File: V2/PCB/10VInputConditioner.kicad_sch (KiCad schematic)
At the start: 3 parts

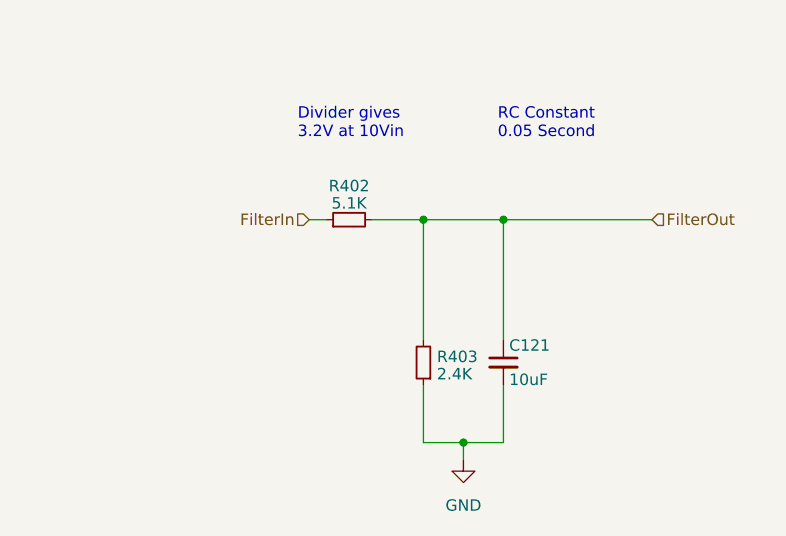
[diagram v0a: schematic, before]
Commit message: Changed ADC divider
Changed ADC divider to give 1.9v for 10V in this matches up with the 2.048v input range on the ADC
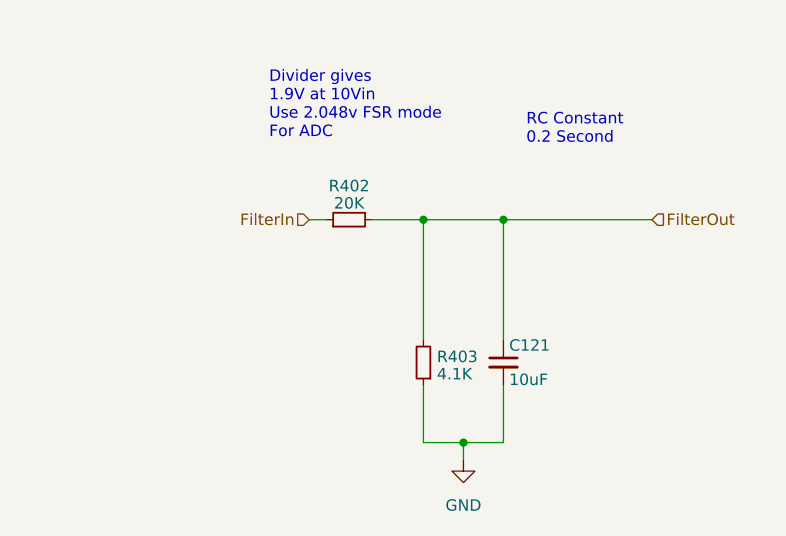
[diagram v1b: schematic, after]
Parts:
- R402: value 5.1K -> 20K
- R403: value 2.4K -> 4.1K
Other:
- note added: "Divider gives 1.9V at 10Vin Use 2.048v FSR mode For ADC"
- note added: "RC Constant 0.2 Second"
- note removed: "Divider gives 3.2V at 10Vin"
- note removed: "RC Constant 0.05 Second"
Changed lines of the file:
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@@
     (stroke (width 0) (type default))
   )
-  (text "Divider gives\n3.2V at 10Vin" (at 100.965 74.93 0)
+  (text "Divider gives\n1.9V at 10Vin\nUse 2.048v FSR mode\nFor ADC"
+    (at 97.79 74.93 0)
     (effects (font (size 1.27 1.27)) (justify left bottom))
   )
-  (text "RC Constant \n0.05 Second" (at 123.19 74.93 0)
+  (text "RC Constant \n0.2 Second" (at 126.365 75.565 0)
     (effects (font (size 1.27 1.27)) (justify left bottom))
   )
@@
       (effects (font (size 1.27 1.27)) (justify right))
     )
-    (property "Value" "2.4K" (at 116.4336 100.9723 0)
+    (property "Value" "4.1K" (at 116.4336 100.9723 0)
       (effects (font (size 1.27 1.27)) (justify right))
     )
@@
       (effects (font (size 1.27 1.27)))
     )
-    (property "Value" "5.1K" (at 106.68 81.9945 90)
+    (property "Value" "20K" (at 106.68 81.9945 90)
       (effects (font (size 1.27 1.27)))
     )

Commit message: Schematic "Finished"
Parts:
- removed R402: 20K, symbol Device:R_Small
- added R113: 10K, Resistor_SMD:R_0805_2012Metric, symbol PGD-Library:R_Small
- added RV1601: 1K, Potentiometer_THT:Potentiometer_Bourns_3296Y_Vertical, symbol Device:R_Potentiometer_Trim
- R502: renamed from R403; value 4.1K -> 2K7; footprint (none) -> Resistor_SMD:R_0805_2012Metric; JLC Part (none) -> Basic Part; LCSC Part (none) -> C17530
- renumbered C121 to C501
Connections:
- net FilterIn: now also R113.2
- net FilterOut: now also RV1601.1, RV1601.2
- new net: R113.1, RV1601.3
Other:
- note added: "Divider gives ~ 2V at 10Vin with 10.7 and 2.7 Use 2.048v FSR mode For ADC"
- note removed: "Divider gives 1.9V at 10Vin Use 2.048v FSR mode For ADC"
